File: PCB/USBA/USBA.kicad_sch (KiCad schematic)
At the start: 23 parts, among them J1 USB_A, J2 Shelly, J3 USB-PROG, J4 Conn_01x03_Socket, SW1 SW_Push, U2 ESP32-S3-MINI-1, U5 MD8942, U8 VEML6040

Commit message: Tweak layout
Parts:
- removed J2: Shelly, RevK:Shelly, symbol RevK:Shelly
- removed J3: USB-PROG, RevK:USB-PROG, symbol RevK:USB-PROG
- C6: value 10uF 50V -> 10uF 35V; LCSC Part # C1591 -> C194427
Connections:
- net +3.3V: now also D1.2 (+)
- net GND: no longer U2.17 (GPIO13)
- net VBUS: no longer D1.2 (+)
- net at D1.1 (O): no longer J4.2 (Pin_2)
- net LED renamed LED1
- new net LED2: J4.2 (Pin_2), U2.17 (GPIO13)
- no-connect marks 22 -> 26
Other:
- moved on the sheet: C3, J4, R1

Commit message: Mic
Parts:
- removed U8: VEML6040, RevK:VEML6040, symbol RevK:VEML6040
- added MK1: MEMS_Microphone, RevK:LMA2718T421, symbol RevK:MEMS_Microphone
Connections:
- net SCL is gone; now on net MIC: U2.29 (GPIO34)
- net +3.3V: now also MK1.4 (VDD)
- net GND: now also MK1.2 (GND), MK1.3 (GND)
- net MIC: now reaches U2.12 (GPIO8)
- net MIC: now also MK1.1 (-)
- net SDA: no longer names the net of U2.30 (GPIO48)
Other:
- moved on the sheet: C6, C7, C8, J1, L2, R10, R11, R9, U5

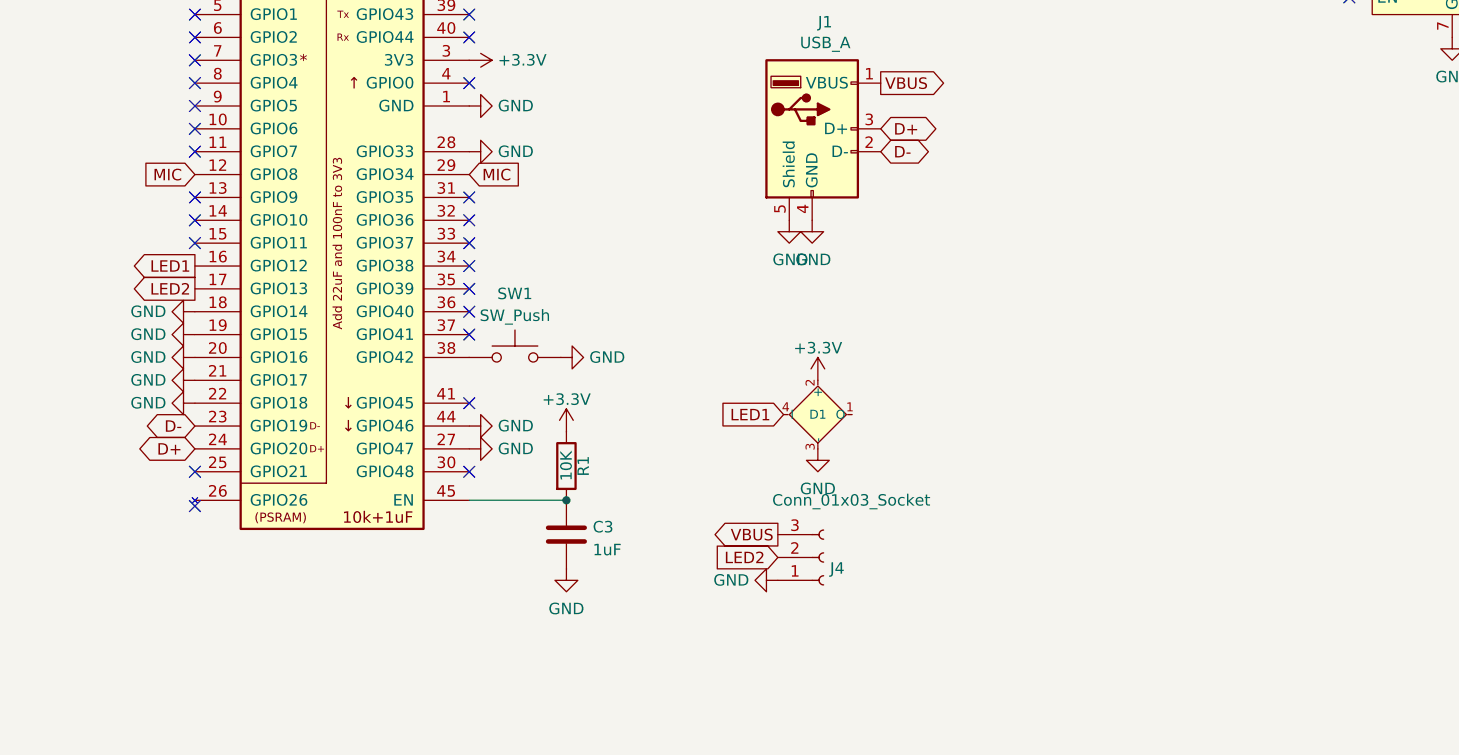
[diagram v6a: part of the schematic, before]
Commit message: Tweak layout for WAGO on back
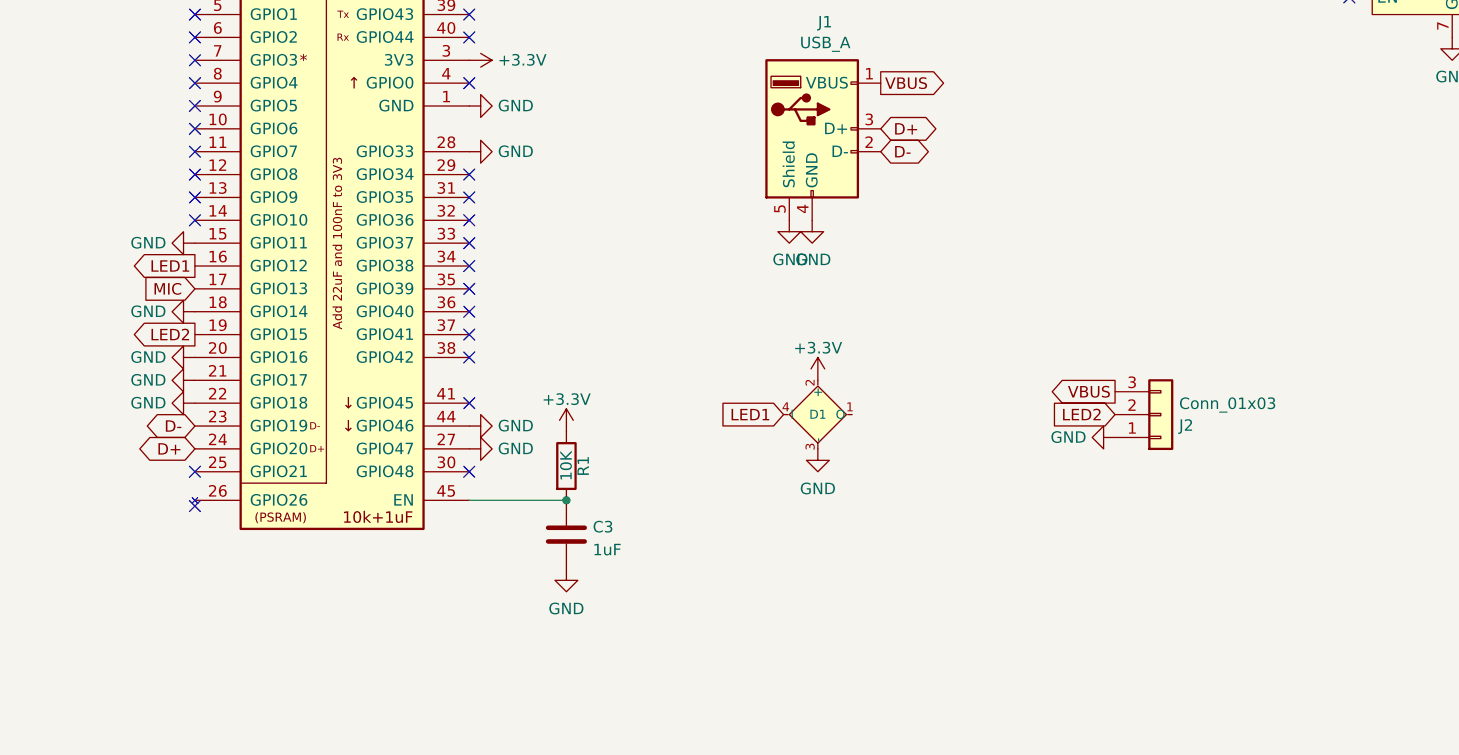
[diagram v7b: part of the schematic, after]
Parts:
- removed J4: Conn_01x03_Socket, RevK:PinHeader_1x03_P2.54mm, symbol Connector:Conn_01x03_Socket
- removed SW1: SW_Push, RevK:TS-1092S-B3D2-G, symbol Switch:SW_Push
- added J2: Conn_01x03, RevK:WAGO-2060-453-998-404, symbol Connector_Generic:Conn_01x03
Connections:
- net GND: now also U2.15 (GPIO11), J2.1 (Pin_1); no longer U2.19 (GPIO15)
- net LED2: now also U2.19 (GPIO15), J2.2 (Pin_2); no longer U2.17 (GPIO13)
- net MIC: now also U2.17 (GPIO13); no longer U2.12 (GPIO8), U2.29 (GPIO34)
- net VBUS: now also J2.3 (Pin_3)
- no-connect marks 26 -> 28
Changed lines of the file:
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@@
 	)
 	(no_connect
+		(at 124.46 70.485)
+	)
+	(no_connect
 		(at 93.98 52.705)
 	)
@@
 	)
 	(no_connect
+		(at 124.46 90.805)
+	)
+	(no_connect
 		(at 124.46 83.185)
 	)
@@
 	)
 	(no_connect
-		(at 93.98 78.105)
+		(at 93.98 70.485)
 	)
 	(no_connect
@@
 	(global_label "LED2"
 		(shape input)
-		(at 158.75 113.03 180)
+		(at 196.215 97.155 180)
 		(fields_autoplaced yes)
 		(effects
@@
 		)
 		(property "Intersheetrefs" "${INTERSHEET_REFS}"
-			(at 151.7624 113.03 0)
+			(at 189.2274 97.155 0)
 			(effects
 				(font
@@
 	(global_label "LED2"
 		(shape output)
-		(at 93.98 83.185 180)
+		(at 93.98 88.265 180)
 		(fields_autoplaced yes)
 		(effects
@@
 		)
 		(property "Intersheetrefs" "${INTERSHEET_REFS}"
-			(at 86.9924 83.185 0)
+			(at 86.9924 88.265 0)
 			(effects
 				(font
@@
 		)
 	)
-	(global_label "MIC"
-		(shape input)
-		(at 124.46 70.485 0)
-		(fields_autoplaced yes)
-		(effects
-			(font
-				(size 1.27 1.27)
-			)
-			(justify left)
-		)
-		(property "Intersheetrefs" "${INTERSHEET_REFS}"
-			(at 130.1172 70.485 0)
-			(effects
-				(font
-					(size 1.27 1.27)
-				)
-				(justify left)
-				(hide yes)
-			)
-		)
-	)
 	(global_label "D-"
 		(shape bidirectional)
@@
 	(global_label "VBUS"
 		(shape output)
-		(at 158.75 110.49 180)
+		(at 196.215 94.615 180)
 		(fields_autoplaced yes)
 		(effects
@@
 		)
 		(property "Intersheetrefs" "${INTERSHEET_REFS}"
-			(at 151.5204 110.49 0)
+			(at 188.9854 94.615 0)
 			(effects
 				(font
@@
 	(global_label "MIC"
 		(shape input)
-		(at 93.98 70.485 180)
+		(at 93.98 83.185 180)
 		(fields_autoplaced yes)
 		(effects
@@
 		)
 		(property "Intersheetrefs" "${INTERSHEET_REFS}"
-			(at 88.3228 70.485 0)
+			(at 88.3228 83.185 0)
 			(effects
 				(font
@@
 	(symbol
 		(lib_id "power:GND")
-		(at 158.75 115.57 270)
+		(at 196.215 99.695 270)
 		(unit 1)
 		(exclude_from_sim no)
@@
 		(fields_autoplaced yes)
 		(property "Reference" "#PWR014"
-			(at 152.4 115.57 0)
+			(at 189.865 99.695 0)
 			(effects
 				(font
@@
 		)
 		(property "Value" "GND"
-			(at 155.5751 115.57 90)
+			(at 193.0401 99.695 90)
 			(effects
 				(font
@@
 		)
 		(property "Footprint" ""
-			(at 158.75 115.57 0)
+			(at 196.215 99.695 0)
 			(effects
 				(font
@@
 		)
 		(property "Datasheet" ""
-			(at 158.75 115.57 0)
+			(at 196.215 99.695 0)
 			(effects
 				(font
@@
 		)
 		(property "Description" "Power symbol creates a global label with name \"GND\" , ground"
-			(at 158.75 115.57 0)
+			(at 196.215 99.695 0)
 			(effects
 				(font
@@
 	(symbol
 		(lib_id "power:GND")
-		(at 93.98 88.265 270)
+		(at 93.98 78.105 270)
 		(unit 1)
 		(exclude_from_sim no)
@@
 		(fields_autoplaced yes)
 		(property "Reference" "#PWR020"
-			(at 87.63 88.265 0)
+			(at 87.63 78.105 0)
 			(effects
 				(font
@@
 		)
 		(property "Value" "GND"
-			(at 90.8051 88.265 90)
+			(at 90.8051 78.105 90)
 			(effects
 				(font
@@
 		)
 		(property "Footprint" ""
-			(at 93.98 88.265 0)
+			(at 93.98 78.105 0)
 			(effects
 				(font
@@
 		)
 		(property "Datasheet" ""
-			(at 93.98 88.265 0)
+			(at 93.98 78.105 0)
 			(effects
 				(font
@@
 		)
 		(property "Description" "Power symbol creates a global label with name \"GND\" , ground"
-			(at 93.98 88.265 0)
+			(at 93.98 78.105 0)
 			(effects
 				(font
@@
 	)
 	(symbol
-		(lib_id "power:GND")
-		(at 134.62 90.805 90)
-		(unit 1)
-		(exclude_from_sim no)
-		(in_bom yes)
-		(on_board yes)
-		(dnp no)
-		(fields_autoplaced yes)
-		(property "Reference" "#PWR025"
-			(at 140.97 90.805 0)
-			(effects
-				(font
-					(size 1.27 1.27)
-				)
-				(hide yes)
-			)
-		)
-		(property "Value" "GND"
-			(at 137.7949 90.805 90)
-			(effects
-				(font
-					(size 1.27 1.27)
-				)
-				(justify right)
-			)
-		)
-		(property "Footprint" ""
-			(at 134.62 90.805 0)
-			(effects
-				(font
-					(size 1.27 1.27)
-				)
-				(hide yes)
-			)
-		)
-		(property "Datasheet" ""
-			(at 134.62 90.805 0)
-			(effects
-				(font
-					(size 1.27 1.27)
-				)
-				(hide yes)
-			)
-		)
-		(property "Description" "Power symbol creates a global label with name \"GND\" , ground"
-			(at 134.62 90.805 0)
-			(effects
-				(font
-					(size 1.27 1.27)
-				)
-				(hide yes)
-			)
-		)
-		(pin "1"
-		)
-		(instances
-			(project "USBA"
-				(path "/2d210a96-f81f-42a9-8bf4-1b43c11086f3"
-					(reference "#PWR025")
-					(unit 1)
-				)
-			)
-		)
-	)
-	(symbol
 		(lib_id "RevK:Hidden")
 		(at 254.635 45.085 0)
@@
 	)
 	(symbol
-		(lib_id "Switch:SW_Push")
-		(at 129.54 90.805 0)
-		(unit 1)
-		(exclude_from_sim no)
-		(in_bom no)
-		(on_board yes)
-		(dnp no)
-		(fields_autoplaced yes)
-		(property "Reference" "SW1"
-			(at 129.54 83.7397 0)
-			(effects
-				(font
-					(size 1.27 1.27)
-				)
-			)
-		)
-		(property "Value" "SW_Push"
-			(at 129.54 86.1639 0)
-			(effects
-				(font
-					(size 1.27 1.27)
-				)
-			)
-		)
-		(property "Footprint" "RevK:TS-1092S-B3D2-G"
-			(at 129.54 85.725 0)
-			(effects
-				(font
-					(size 1.27 1.27)
-				)
-				(hide yes)
-			)
-		)
-		(property "Datasheet" "~"
-			(at 129.54 85.725 0)
-			(effects
-				(font
-					(size 1.27 1.27)
-				)
-				(hide yes)
-			)
-		)
-		(property "Description" "Push button switch, generic, two pins"
-			(at 129.54 90.805 0)
-			(effects
-				(font
-					(size 1.27 1.27)
-				)
-				(hide yes)
-			)
-		)
-		(pin "1"
-		)
-		(pin "2"
-		)
-		(instances
-			(project "USBA"
-				(path "/2d210a96-f81f-42a9-8bf4-1b43c11086f3"
-					(reference "SW1")
-					(unit 1)
-				)
-			)
-		)
-	)
-	(symbol
 		(lib_id "RevK:ESP32-S3-MINI-1-N4R2")
 		(at 109.22 79.375 0)
@@
 	)
 	(symbol
+		(lib_id "Connector_Generic:Conn_01x03")
+		(at 201.295 97.155 0)
+		(mirror x)
+		(unit 1)
+		(exclude_from_sim no)
+		(in_bom yes)
+		(on_board yes)
+		(dnp no)
+		(property "Reference" "J2"
+			(at 203.327 98.3672 0)
+			(effects
+				(font
+					(size 1.27 1.27)
+				)
+				(justify left)
+			)
+		)
+		(property "Value" "Conn_01x03"
+			(at 203.327 95.9429 0)
+			(effects
+				(font
+					(size 1.27 1.27)
+				)
+				(justify left)
+			)
+		)
+		(property "Footprint" "RevK:WAGO-2060-453-998-404"
+			(at 201.295 97.155 0)
+			(effects
+				(font
+					(size 1.27 1.27)
+				)
+				(hide yes)
+			)
+		)
+		(property "Datasheet" "~"
+			(at 201.295 97.155 0)
+			(effects
+				(font
+					(size 1.27 1.27)
+				)
+				(hide yes)
+			)
+		)
+		(property "Description" "Generic connector, single row, 01x03, script generated (kicad-library-utils/schlib/autogen/connector/)"
+			(at 201.295 97.155 0)
+			(effects
+				(font
+					(size 1.27 1.27)
+				)
+				(hide yes)
+			)
+		)
+		(pin "3"
+		)
+		(pin "2"
+		)
+		(pin "1"
+		)
+		(instances
+			(project ""
+				(path "/2d210a96-f81f-42a9-8bf4-1b43c11086f3"
+					(reference "J2")
+					(unit 1)
+				)
+			)
+		)
+	)
+	(symbol
 		(lib_id "power:+3.3V")
 		(at 124.46 57.785 270)
@@
 					(unit 1)
 				)
-			)
-		)
-	)
-	(symbol
-		(lib_id "Connector:Conn_01x03_Socket")
-		(at 163.83 113.03 0)
-		(mirror x)
-		(unit 1)
-		(exclude_from_sim no)
-		(in_bom no)
-		(on_board yes)
-		(dnp no)
-		(property "Reference" "J4"
-			(at 164.5412 114.2421 0)
-			(effects
-				(font
-					(size 1.27 1.27)
-				)
-				(justify left)
-			)
-		)
-		(property "Value" "Conn_01x03_Socket"
-			(at 158.115 106.68 0)
-			(effects
-				(font
-					(size 1.27 1.27)
-				)
-				(justify left)
-			)
-		)
-		(property "Footprint" "RevK:PinHeader_1x03_P2.54mm"
-			(at 163.83 113.03 0)
-			(effects
-				(font
-					(size 1.27 1.27)
-				)
-				(hide yes)
-			)
-		)
-		(property "Datasheet" "~"
-			(at 163.83 113.03 0)
-			(effects
-				(font
-					(size 1.27 1.27)
-				)
-				(hide yes)
-			)
-		)
-		(property "Description" "Generic connector, single row, 01x03, script generated"
-			(at 163.83 113.03 0)
-			(effects
-				(font
-					(size 1.27 1.27)
-				)
-				(hide yes)
-			)
-		)
-		(pin "1"
-		)
-		(pin "2"
-		)
-		(pin "3"
-		)
-		(instances
-			(project "USBA"
-				(path "/2d210a96-f81f-42a9-8bf4-1b43c11086f3"
-					(reference "J4")
-					(unit 1)
-				)

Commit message: Re do GPIO
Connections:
- net LED2: now also U2.5 (GPIO1); no longer U2.19 (GPIO15)
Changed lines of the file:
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@@
 	)
 	(no_connect
-		(at 93.98 52.705)
+		(at 93.98 88.265)
 	)
 	(no_connect
@@
 	(global_label "LED2"
 		(shape output)
-		(at 93.98 88.265 180)
-		(fields_autoplaced yes)
-		(effects
-			(font
-				(size 1.27 1.27)
-			)
-			(justify right)
-		)
-		(property "Intersheetrefs" "${INTERSHEET_REFS}"
-			(at 86.9924 88.265 0)
-			(effects
-				(font
+		(at 93.98 52.705 180)
+		(fields_autoplaced yes)
+		(effects
+			(font
+				(size 1.27 1.27)
+			)
+			(justify right)
+		)
+		(property "Intersheetrefs" "${INTERSHEET_REFS}"
+			(at 86.9924 52.705 0)
+			(effects
+				(font
